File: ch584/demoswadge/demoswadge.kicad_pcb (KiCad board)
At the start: 2 copper layers, 63 parts, among them J1 SAO, J2 PJ-307C, P1 USB_C_Plug_USB2.0, SW1 TS-1187A-B-A-B, SW2 TS-1187A-B-A-B, SW3 TS-1187A-B-A-B, SW4 TS-1187A-B-A-B, SW5 TS-1187A-B-A-B, SW6 TS-1187A-B-A-B, SW7 TS-1187A-B-A-B, U2 SM5701_2.2V, U3 XC6206PxxxMR, U4 XT1861B332MR-G, U6 LSM6DSL, Y1 32MHz, Y2 32.768kHz

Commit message: Bump demoswadge
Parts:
- added C21: 10μF, Capacitor_SMD:C_0603_1608Metric, F.Cu at (114.2, 82.3)
- added C22: 4.7nF, cnhardware:R_0402_1005Metric_COMPACT, F.Cu at (100.0, 107.7)
- added Q1: PMOS, Swadge_Parts:SOT-23, F.Cu at (68.3, 116.5)
- added Q2: PMOS, Swadge_Parts:SOT-23, F.Cu at (75.2, 115.4)
- added R4: 1MΩ, cnhardware:R_0402_1005Metric_COMPACT, F.Cu at (67.5, 121.7)
- added R5: 1MΩ, cnhardware:R_0402_1005Metric_COMPACT, F.Cu at (67.5, 123.7)
- C15, C4, C5: footprint Swadge_Parts:C_0603_1608Metric -> Capacitor_SMD:C_0402_1005Metric
- C9: footprint Swadge_Parts:C_0603_1608Metric -> cnhardware:R_0402_1005Metric_COMPACT
- R1, R10, R13, R14, R2, R27, R28, R3, R6, R7, R8, R9: footprint Swadge_Parts:R_0603_1608Metric -> cnhardware:R_0402_1005Metric_COMPACT
- moved U4 80.2 mm to (75.5, 106.7), turned to 60 degrees
- moved C18 79.7 mm to (72.6, 109.8), turned to 60 degrees
- moved L3 70.0 mm to (120.7, 106.2)
- moved C16 68.1 mm to (123.9, 105.1)
- moved C12 67.4 mm to (124.0, 101.2)
- moved L4 66.8 mm to (120.8, 101.4)
- moved J2 60.3 mm to (136.0, 104.5), turned to -90 degrees
- moved C17 57.1 mm to (101.7, 108.2), turned to 60 degrees
- moved C15 56.6 mm to (117.8, 121.2)
- moved C3 55.0 mm to (95.7, 99.8), turned to -120 degrees
- moved MK1 53.3 mm to (76.7, 82.8)
- moved U6 52.7 mm to (98.9, 105.7)
- moved C6 51.6 mm to (79.6, 112.8), turned to 150 degrees
- moved U3 50.2 mm to (114.0, 85.9), turned to 90 degrees
- moved L2 49.5 mm to (82.4, 113.4), turned to 60 degrees
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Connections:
- C18 pad 1: BATT -> Net-(Q1-D)
- C6 pad 1: BATT -> Net-(Q2-D)
- L2 pad 1: BATT -> Net-(Q2-D)
- L5 pad 1: BATT -> Net-(Q1-D)
- R10 pad 1: GND -> +2V2
- R2 pad 2: +2V2 -> MICON
- R6 pad 1: +2V2 -> IMUON
- R7 pad 1: GND -> +2V2
- R8 pad 1: GND -> +2V2
- R9 pad 1: GND -> +2V2
- SW1 pad 2: MEAS -> GND
- SW2 pad 2: MEAS -> GND
- SW3 pad 2: MEAS -> GND
- SW4 pad 2: MEAS -> GND
- SW5 pad 2: MEAS -> GND
- SW6 pad 2: MEAS -> GND
- SW7 pad 2: MEAS -> GND
- U1 pad 10: unconnected-(U1-PB16-Pad10) -> IMUON
- U1 pad 29: unconnected-(U1-PB19-Pad29) -> MICON
- U1 pad 30: unconnected-(U1-PB18-Pad30) -> OLEDCS
- U1 pad 37: OLEDCS -> MIC
- U6 pad 12: +2V2 -> IMUON
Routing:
- net Net-(U1-VCIA): track 0.00 -> 3.49 mm
- net Net-(U1-VDCID): track 0.00 -> 2.26 mm
- net Net-(U1-VINTA): track 0.00 -> 2.10 mm
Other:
- board outline added: 10.7 x 10.7 mm

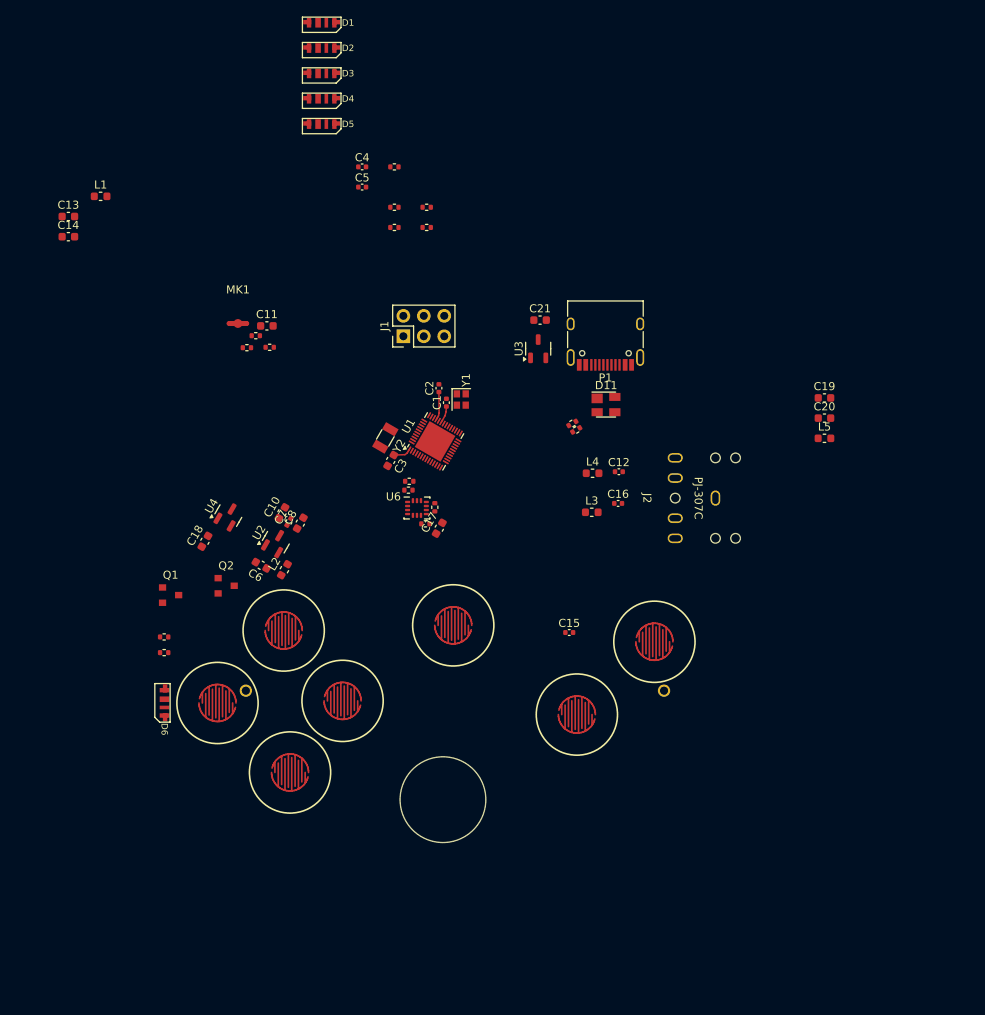
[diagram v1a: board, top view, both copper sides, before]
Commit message: Update submodules Update demo swadge Update kicad parts Update new frogswadge
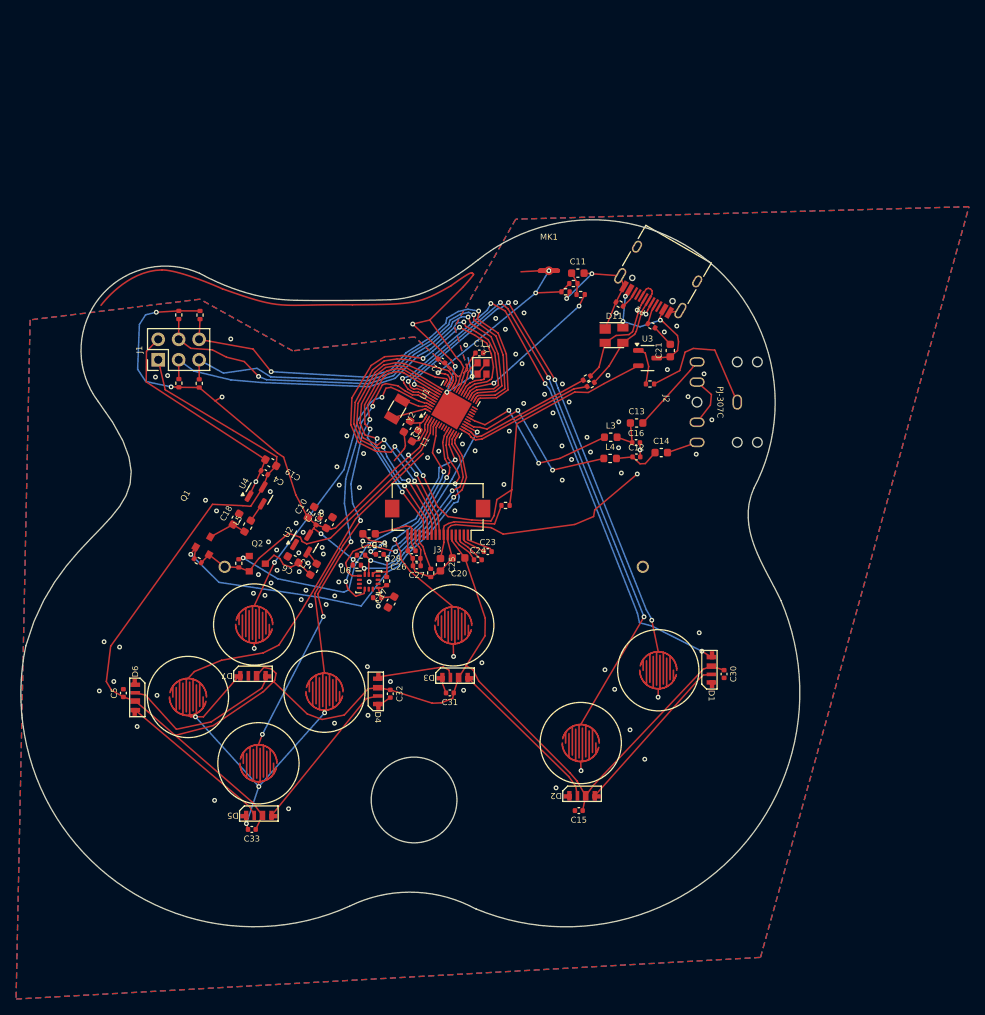
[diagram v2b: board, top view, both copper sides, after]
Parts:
- added C23: 1μF, Capacitor_SMD:C_0402_1005Metric, F.Cu at (107.7, 111.1)
- added C24: 1μF, Capacitor_SMD:C_0402_1005Metric, F.Cu at (106.5, 112.2)
- added C25: 10μF, Capacitor_SMD:C_0603_1608Metric, F.Cu at (101.8, 112.8)
- added C26: 1μF, Capacitor_SMD:C_0402_1005Metric, F.Cu at (98.9, 112.0)
- added C27: 1μF, Capacitor_SMD:C_0402_1005Metric, F.Cu at (98.9, 112.9)
- added C28: 1μF, Capacitor_SMD:C_0402_1005Metric, F.Cu at (98.3, 111.0)
- added C29: 10μF, Capacitor_SMD:C_0603_1608Metric, F.Cu at (93.0, 108.9)
- added C30: 1μF, Capacitor_SMD:C_0402_1005Metric, F.Cu at (137.1, 126.3)
- added C31: 1μF, Capacitor_SMD:C_0402_1005Metric, F.Cu at (103.0, 128.7)
- added C32: 1μF, Capacitor_SMD:C_0402_1005Metric, F.Cu at (95.6, 128.8)
- added C33: 1μF, Capacitor_SMD:C_0402_1005Metric, F.Cu at (78.4, 145.7)
- added C34: 1μF, Capacitor_SMD:C_0402_1005Metric, F.Cu at (94.3, 111.5)
- added D7: SK6812-SIDE-A, Swadge_Parts:SK6812_SIDE_2, F.Cu at (78.5, 126.6)
- added J3: RB130-2864KSWXG22, Connector_FFC-FPC:Hirose_FH12-16S-0.5SH_1x16-1MP_P0.50mm_Horizontal, F.Cu at (101.5, 107.2)
- added R11: 5.1kΩ, cnhardware:R_0402_1005Metric_COMPACT, F.Cu at (72.0, 81.7)
- added R12: 5.1kΩ, cnhardware:R_0402_1005Metric_COMPACT, F.Cu at (71.8, 90.2)
- added R15: OLEDSHUNT, cnhardware:R_0402_1005Metric_COMPACT, F.Cu at (109.9, 105.4)
- added R16: 560kΩ, cnhardware:R_0402_1005Metric_COMPACT, F.Cu at (100.6, 113.8)
- MK1: value Microphone -> 56db
- moved D2 98.4 mm to (119.4, 141.5), turned to 180 degrees
- moved D1 93.9 mm to (135.5, 125.8), turned to -90 degrees
- moved D5 86.3 mm to (79.3, 143.9), turned to 180 degrees
- moved C14 78.4 mm to (129.3, 98.8)
- moved D3 76.9 mm to (103.7, 126.8), turned to 180 degrees
- moved C13 75.2 mm to (126.2, 95.1)
- moved D4 74.0 mm to (94.0, 128.5), turned to -90 degrees
- moved L5 72.5 mm to (77.9, 108.0), turned to 60 degrees
- moved C5 69.6 mm to (62.4, 128.7), turned to 90 degrees
- moved C19 69.3 mm to (80.8, 100.1), turned to 150 degrees
- moved L1 49.2 mm to (98.7, 96.7), turned to -120 degrees
- moved C20 48.7 mm to (104.1, 111.9), turned to 180 degrees
- moved R3 41.7 mm to (127.9, 90.3), turned to 180 degrees
- moved C9 40.2 mm to (117.4, 78.8)
- moved R1 40.0 mm to (118.4, 77.8)
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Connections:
- D6 pad 2: unconnected-(D6-VDD-Pad2) -> +3V3
- D6 pad 3: unconnected-(D6-OUT-Pad3) -> Net-(D6-OUT)
- R8 pad 2: SDA_SAO -> SCL_SAO
- U1 pad 49: (no net) -> GND
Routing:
- net +3V3: track 0.00 -> 200.7 mm
- net GND: track 0.00 -> 198.6 mm, vias 0 -> 112
- net +2V2: track 0.00 -> 130.7 mm, vias 0 -> 8
- net B3: track 0.00 -> 78.0 mm, vias 0 -> 4
- net LED: track 0.00 -> 73.9 mm, vias 0 -> 4
- net B4: track 0.00 -> 66.3 mm, vias 0 -> 4
- net SAOG2: track 0.00 -> 57.6 mm, vias 0 -> 2
- net SCL_SAO: track 0.00 -> 57.6 mm, vias 0 -> 2
- net B1: track 0.00 -> 56.2 mm, vias 0 -> 4
- net SAOG1: track 0.00 -> 55.5 mm, vias 0 -> 1
- net SDA_SAO: track 0.00 -> 55.2 mm, vias 0 -> 1
- net OLEDCS: track 0.00 -> 53.5 mm, vias 0 -> 4
- net PGM_TCK: track 0.00 -> 52.9 mm, vias 0 -> 2
- net B5: track 0.00 -> 47.4 mm, vias 0 -> 2
- net B2: track 0.00 -> 43.9 mm
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- added copper zone on B.Cu, net GND
- added copper zone on F.Cu, net GND
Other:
- board size 10.7 x 10.7 mm -> 96.8 x 87.9 mm

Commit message: Bump design
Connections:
- net Net-(Q1-D) renamed BATTMID33
- net Net-(U2-LX) renamed BATTLX22
- net Net-(U4-LX) renamed BATTLX33
- C6 pad 1: Net-(Q2-D) -> BATTMID22
- L2 pad 1: Net-(Q2-D) -> BATTMID22
- Q2 pad 3: Net-(Q2-D) -> BATTMID22
- SW7 pad 1: B6 -> PGM_TIO
- U1 pad 4: BATT -> BATTMID22
- U1 pad 6: B6 -> unconnected-(U1-PA9-Pad6)
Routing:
- net BATTMID22: track 0.00 -> 36.5 mm
- net BATT: track 39.2 -> 7.00 mm
- net B6: track 28.5 -> 0.00 mm, vias 2 -> 0
- net PGM_TIO: track 41.6 -> 54.4 mm, vias 2 -> 3
- net GND: track 198.6 -> 210.6 mm, vias 112 -> 253
- net Net-(Q2-D): track 7.33 -> 0.00 mm
- net B2: track 43.9 -> 46.5 mm
- net +2V2: track 130.7 -> 129.7 mm, vias 8 -> 7

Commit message: update froggy/test
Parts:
- removed J3: RB130-2864KSWXG22, Connector_FFC-FPC:Hirose_FH12-16S-0.5SH_1x16-1MP_P0.50mm_Horizontal
- moved R2 43.7 mm to (75.8, 83.7), turned to -90 degrees
- moved R1 41.5 mm to (77.2, 82.8), turned to -90 degrees
- moved C9 41.4 mm to (76.1, 81.8), turned to 90 degrees
- moved C11 41.0 mm to (78.5, 83.4), turned to -90 degrees
- moved MK1 37.2 mm to (78.2, 79.3), turned to -90 degrees
- moved D7 17.0 mm to (81.1, 109.8), turned to 0 degrees
- moved C8 16.5 mm to (75.5, 96.8), turned to 90 degrees
- moved C10 16.0 mm to (72.9, 96.8), turned to 90 degrees
- moved C7 16.0 mm to (74.2, 97.3), turned to 90 degrees
- moved L2 14.5 mm to (76.5, 102.3), turned to 90 degrees
- moved U2 14.5 mm to (74.1, 100.3), turned to 90 degrees
- moved C14 13.8 mm to (119.1, 108.1)
- moved C13 13.5 mm to (119.0, 106.6)
- moved C6 13.3 mm to (73.9, 103.0), turned to 180 degrees
- moved C19 13.0 mm to (68.3, 96.4), turned to 180 degrees
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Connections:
- U1 pad 10: IMUON -> unconnected-(U1-PB16-Pad10)
- U1 pad 19: unconnected-(U1-PB5-Pad19) -> IMUON
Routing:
- net GND: track 210.6 -> 0.00 mm, vias 253 -> 0
- net +3V3: track 201.2 -> 0.00 mm
- net +2V2: track 129.7 -> 0.00 mm, vias 7 -> 0
- net B3: track 78.0 -> 0.00 mm, vias 4 -> 0
- net LED: track 73.9 -> 0.00 mm, vias 4 -> 0
- net B4: track 66.3 -> 0.00 mm, vias 4 -> 0
- net SAOG2: track 57.6 -> 0.00 mm, vias 2 -> 0
- net SCL_SAO: track 57.6 -> 0.00 mm, vias 2 -> 0
- net B1: track 56.2 -> 0.00 mm, vias 4 -> 0
- net SAOG1: track 55.5 -> 0.00 mm, vias 1 -> 0
- net SDA_SAO: track 55.2 -> 0.00 mm, vias 1 -> 0
- net PGM_TIO: track 54.4 -> 0.00 mm, vias 3 -> 0
- net OLEDCS: track 53.5 -> 0.00 mm, vias 4 -> 0
- net PGM_TCK: track 52.9 -> 0.00 mm, vias 2 -> 0
- net B5: track 47.3 -> 0.00 mm, vias 2 -> 0
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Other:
- board size 96.8 x 87.9 mm -> 10.7 x 10.7 mm

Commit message: Bump demoswadge
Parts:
- moved R3 19.2 mm to (122.0, 108.5), turned to -90 degrees
- moved C30 11.3 mm to (128.8, 112.2), turned to 0 degrees
- moved C31 11.2 mm to (111.4, 120.6), turned to -90 degrees
- moved R15 10.0 mm to (103.6, 113.2)
- moved D3 9.16 mm to (110.0, 120.4), turned to -90 degrees
- moved D1 9.07 mm to (128.6, 113.8), turned to 0 degrees
- moved R14 8.34 mm to (118.9, 96.2), turned to 90 degrees
- moved J2 7.91 mm to (134.2, 96.3), turned to -110 degrees
- moved D11 7.56 mm to (120.2, 93.3), turned to 0 degrees
- moved C18 7.52 mm to (74.9, 98.4)
- moved C10 7.52 mm to (78.7, 92.1)
- moved C8 7.52 mm to (81.4, 92.1)
- moved L2 7.52 mm to (82.4, 97.6)
- moved Q1 7.52 mm to (75.0, 100.8)
- moved Q2 7.52 mm to (79.9, 100.8)
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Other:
- board size 10.7 x 10.7 mm -> 81.5 x 72.2 mm

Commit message: Bump desing for 570+584
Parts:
- added C35: 1μF, Capacitor_SMD:C_0402_1005Metric, F.Cu at (81.9, 107.9)
- added J3: RB130-2864KSWXG22, cnhardware:FPC-16-P0.50mm-HC-FPC-05-09-16RLTAG-TOP-AND-BOTTOM, F.Cu at (100.9, 105.0)
- added TP1: BATT, TestPoint:TestPoint_Pad_D1.0mm, B.Cu at (69.2, 112.9)
- added TP2: VDCID, TestPoint:TestPoint_Pad_D1.0mm, B.Cu at (99.0, 95.0)
- added TP3: OLEDVDD, TestPoint:TestPoint_Pad_D1.0mm, B.Cu at (102.0, 104.6)
- added TP4: GND, TestPoint:TestPoint_Pad_D1.0mm, B.Cu at (131.8, 105.8)
- moved C15 15.9 mm to (119.4, 121.3), turned to 0 degrees
- moved D2 12.8 mm to (118.8, 123.0), turned to 0 degrees
- moved R2 5.87 mm to (81.2, 81.5), turned to 0 degrees
- moved MK1 5.74 mm to (78.9, 85.0), turned to 90 degrees
- moved C9 5.16 mm to (81.3, 82.5), turned to 180 degrees
- moved L4 4.44 mm to (115.9, 104.1)
- moved C12 4.44 mm to (117.8, 103.9)
- moved C14 4.44 mm to (119.8, 103.7)
- moved C16 4.44 mm to (117.8, 102.0)
- moved L3 4.44 mm to (115.9, 101.8)
- moved C13 4.44 mm to (119.8, 102.2)
- moved R15 4.26 mm to (99.4, 113.7), turned to 180 degrees
- moved R3 4.23 mm to (119.9, 104.9), turned to 180 degrees
- moved R16 2.93 mm to (100.4, 110.9)
- moved C24 2.84 mm to (104.9, 109.8)
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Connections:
- C2 pad 1: Net-(U1-VCIA) -> VDCI
- C3 pad 1: Net-(U1-VDCID) -> VDCI
- L1 pad 1: Net-(U1-VDCID) -> VDCI
- U1 pad 1: Net-(U1-VDCID) -> VDCI
- U1 pad 10: unconnected-(U1-PB16-Pad10) -> NFC-
- U1 pad 35: Net-(U1-VCIA) -> VDCI
- U1 pad 7: unconnected-(U1-PB9-Pad7) -> NFCI
- U1 pad 8: unconnected-(U1-PB8-Pad8) -> NFCM
- U1 pad 9: unconnected-(U1-PB17-Pad9) -> NFC+
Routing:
- net GND: track 0.00 -> 353.5 mm, vias 0 -> 34
- net +3V3: track 0.00 -> 190.9 mm, vias 0 -> 3
- net +2V2: track 0.00 -> 104.0 mm, vias 0 -> 7
- net SCL_SAO: track 0.00 -> 61.0 mm, vias 0 -> 2
- net B4: track 0.00 -> 57.3 mm, vias 0 -> 4
- net B3: track 0.00 -> 57.0 mm, vias 0 -> 4
- net PGM_TIO: track 0.00 -> 55.2 mm, vias 0 -> 3
- net SDA_SAO: track 0.00 -> 52.0 mm, vias 0 -> 3
- net SAOG2: track 0.00 -> 51.9 mm, vias 0 -> 2
- net LED: track 0.00 -> 51.4 mm, vias 0 -> 2
- net B1: track 0.00 -> 49.5 mm, vias 0 -> 2
- net SAOG1: track 0.00 -> 49.3 mm, vias 0 -> 3
- net B5: track 0.00 -> 44.1 mm, vias 0 -> 2
- net B2: track 0.00 -> 41.3 mm, vias 0 -> 2
- net OLEDRST: track 0.00 -> 37.1 mm, vias 0 -> 4
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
